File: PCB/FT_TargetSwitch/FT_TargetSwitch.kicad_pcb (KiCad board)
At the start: 2 copper layers, 73 x 73 mm, 11 parts

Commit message: changed hall, switch
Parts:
- R_PUP1: footprint Resistor_SMD:R_0603_1608Metric_Pad0.98x0.95mm_HandSolder -> Resistor_SMD:R_1206_3216Metric_Pad1.30x1.75mm_HandSolder
- moved D1 26.7 mm to (149.9, 78.7), turned to 180 degrees
- moved D2 14.2 mm to (128.3, 78.7), turned to 0 degrees
- moved Q_OUT1 11.5 mm to (142.2, 78.7), turned to 0 degrees
- moved R_PUP1 2.54 mm to (138.4, 71.1)
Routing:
- net /PASTRHRU_IN: track 7.61 -> 35.7 mm
- net /PASTHRU_OUT: track 68.6 -> 51.7 mm
- net /OUT: track 56.7 -> 69.3 mm
- net /HAL_IN: track 35.1 -> 25.9 mm
- net /Q_UOT_DRAIN: track 5.51 -> 4.18 mm
- net +12V: track 76.8 -> 75.9 mm
- removed copper zone on F.Cu, net GND

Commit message: update pcbs
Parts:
- removed D1, D2: M7, Diode_SMD:D_SMA_Handsoldering
- removed SW_L1, SW_R1: SW_DIP_x02, Button_Switch_THT:SW_DIP_SPSTx02_Slide_9.78x7.26mm_W7.62mm_P2.54mm
- R_PUP1: footprint Resistor_SMD:R_1206_3216Metric_Pad1.30x1.75mm_HandSolder -> Resistor_SMD:R_0603_1608Metric
- moved CON_PASTHRU1 53.2 mm to (126.7, 109.9)
- moved CON_LED1 52.1 mm to (113.6, 112.4)
- moved Q_LED1 50.7 mm to (109.0, 118.5)
- moved R_PUP1 49.7 mm to (117.6, 116.2), turned to 180 degrees
- moved Q_OUT1 47.9 mm to (117.6, 119.8), turned to 180 degrees
- moved CON_HAL1 43.1 mm to (113.7, 129.4)
- moved CON_IO1 41.8 mm to (126.8, 121.8)
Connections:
- CON_IO1 pad 3: /L_OUT -> /OUT
- CON_IO1 pad 4: /R_OUT -> /PASSTHRU_OUT
- CON_PASTHRU1 pad 3: /PASTRHRU_IN -> /PASSTHRU_OUT
- Q_OUT1 pad 3: /Q_UOT_DRAIN -> /OUT
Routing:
- net /OUT: track 69.3 -> 16.3 mm
- net /PASTHRU_OUT: track 51.7 -> 0.00 mm
- net /L_OUT: track 42.5 -> 0.00 mm
- net /PASSTHRU_OUT: track 0.00 -> 41.6 mm
- net /R_OUT: track 37.1 -> 0.00 mm
- net /PASTRHRU_IN: track 35.7 -> 0.00 mm
- net GND: track 0.00 -> 27.6 mm
- net /HAL_IN: track 25.9 -> 14.0 mm
- net +12V: track 75.9 -> 70.8 mm
- net /Q_UOT_DRAIN: track 4.18 -> 0.00 mm
- net /LED_OUT: track 9.95 -> 11.1 mm
- removed copper zone on B.Cu, net GND
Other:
- board size 73 x 73 mm -> 40 x 40 mm
- board text added: "Q1"
- board text added: "Q2"
- board text removed: ">L<"
- board text removed: ">R"
- board text removed: "Firesport timer | Light switch Martin Vejman v1"
- board text removed: "L"
- board text removed: "R"
- board text removed: "R<"

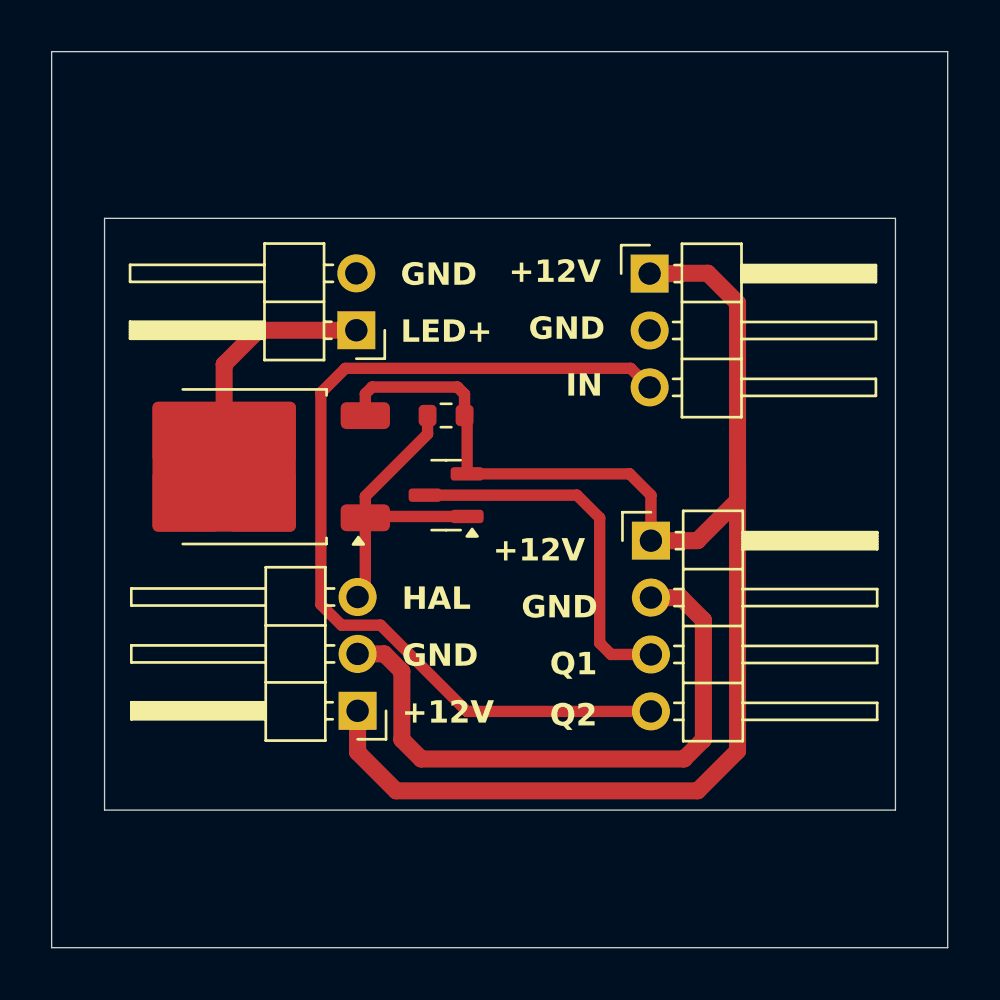
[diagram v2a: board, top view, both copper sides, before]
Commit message: hall and switch done
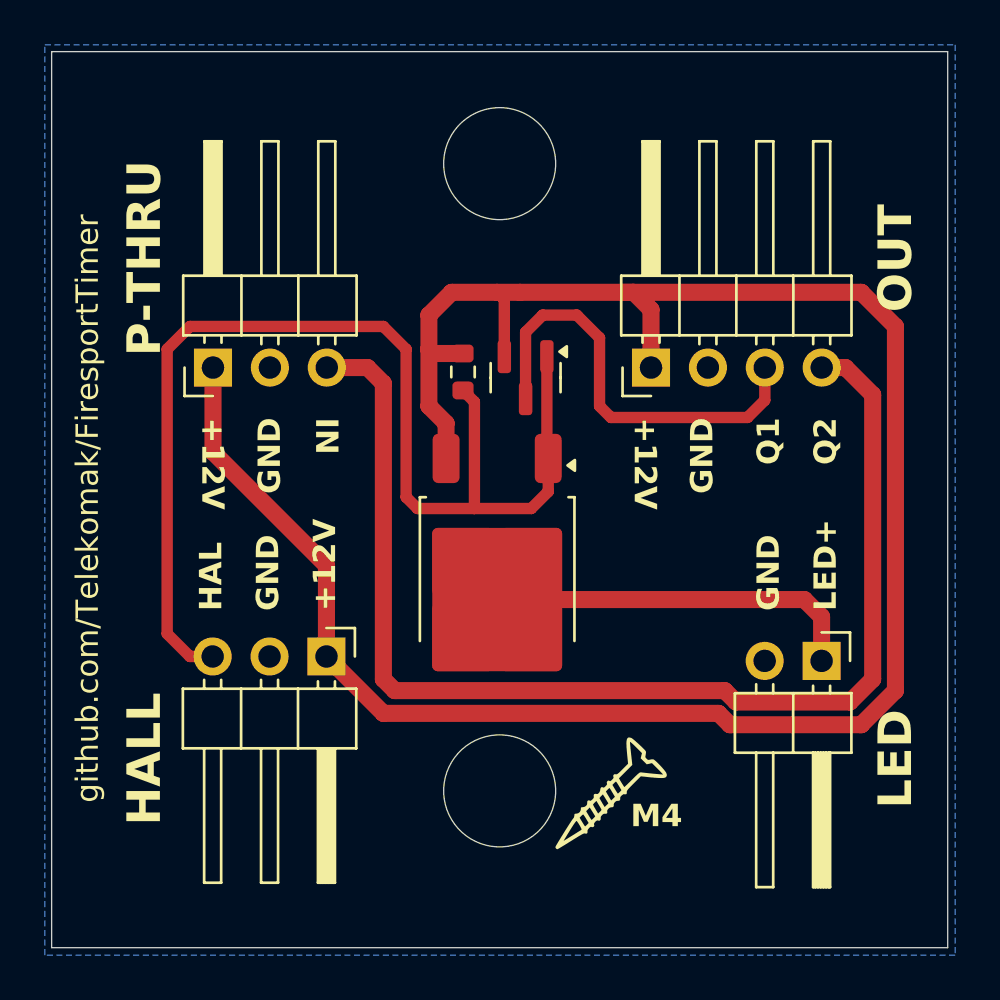
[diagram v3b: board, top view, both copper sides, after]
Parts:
- added G***: LOGO, LOGO, F.Cu at (125.0, 133.1)
- moved CON_LED1 25.5 mm to (134.4, 127.2), turned to -90 degrees
- moved CON_PASTHRU1 19.9 mm to (107.2, 114.1), turned to 90 degrees
- moved Q_LED1 11.9 mm to (119.9, 123.2), turned to -90 degrees
- moved CON_IO1 7.73 mm to (126.8, 114.1), turned to 90 degrees
- moved Q_OUT1 6.33 mm to (121.2, 114.6), turned to -90 degrees
- moved CON_HAL1 2.80 mm to (112.3, 127.0), turned to -90 degrees
- moved R_PUP1 2.08 mm to (118.4, 114.3), turned to -90 degrees
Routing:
- net /HAL_IN: track 14.0 -> 51.7 mm
- net GND: track 27.6 -> 0.00 mm
- net +12V: track 70.8 -> 95.9 mm
- net /PASSTHRU_OUT: track 41.6 -> 54.2 mm
- net /LED_OUT: track 11.1 -> 16.8 mm
- net /OUT: track 16.3 -> 19.4 mm
- added copper zone on B.Cu, net GND
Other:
- outline, holes or cut-outs redrawn
- board text added: "Firesport timer Light switch v1 Martin Vejman"
- board text added: "HALL"
- board text added: "LED"
- board text added: "M4"
- board text added: "OUT"
- board text added: "P-THRU"
- board text added: "github.com/Telekomak/FiresportTimer"

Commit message: final
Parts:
- renumbered CON_IO1 to CON1, CON_PASTHRU1 to CON2, CON_HAL1 to CON3, CON_LED1 to CON4, Q_OUT1 to Q1, Q_LED1 to Q1, R_PUP1 to R1
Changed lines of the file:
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@@
 		(descr "SOT, 3 Pin (https://www.jedec.org/system/files/docs/to-236h.pdf variant AB), generated with kicad-footprint-generator ipc_gullwing_generator.py")
 		(tags "SOT TO_SOT_SMD")
-		(property "Reference" "Q_OUT1"
+		(property "Reference" "Q1"
 			(at 2.794 1.016 180)
 			(layer "F.SilkS")
@@
 		(descr "Through hole angled pin header, 1x02, 2.54mm pitch, 6mm pin length, single row")
 		(tags "Through hole angled pin header THT 1x02 2.54mm single row")
-		(property "Reference" "CON_LED1"
+		(property "Reference" "CON4"
 			(at 4.375 7.625 90)
 			(layer "F.SilkS")
@@
 		(descr "Resistor SMD 0603 (1608 Metric), square (rectangular) end terminal, IPC_7351 nominal, (Body size source: IPC-SM-782 page 72, https://www.pcb-3d.com/wordpress/wp-content/uploads/ipc-sm-782a_amendment_1_and_2.pdf), generated with kicad-footprint-generator")
 		(tags "resistor")
-		(property "Reference" "R_PUP1"
+		(property "Reference" "R1"
 			(at 0 1.524 90)
 			(layer "F.SilkS")
@@
 		(descr "Through hole angled pin header, 1x03, 2.54mm pitch, 6mm pin length, single row")
 		(tags "Through hole angled pin header THT 1x03 2.54mm single row")
-		(property "Reference" "CON_PASTHRU1"
-			(at 4.375 -3.81 270)
+		(property "Reference" "CON2"
+			(at 4.375 -3.81 -90)
 			(layer "F.SilkS")
 			(hide yes)
@@
 		)
 		(property "Value" "Conn_01x03_Pin"
-			(at 4.385 7.35 270)
+			(at 4.385 7.35 -90)
 			(layer "F.Fab")
 			(hide yes)
@@
 		)
 		(fp_text user "${REFERENCE}"
-			(at 2.77 2.54 360)
+			(at 2.77 2.54 0)
 			(layer "F.Fab")
 			(effects
@@
 		(descr "TO-252/DPAK SMD package, http://www.infineon.com/cms/en/product/packages/PG-TO252/PG-TO252-3-1/")
 		(tags "DPAK TO-252 DPAK-3 TO-252-3 SOT-428")
-		(property "Reference" "Q_LED1"
+		(property "Reference" "Q1"
 			(at 5.578 0.254 180)
 			(layer "F.SilkS")
@@
 		(descr "Through hole angled pin header, 1x04, 2.54mm pitch, 6mm pin length, single row")
 		(tags "Through hole angled pin header THT 1x04 2.54mm single row")
-		(property "Reference" "CON_IO1"
-			(at 4.375 10.15 270)
+		(property "Reference" "CON1"
+			(at 4.375 10.15 -90)
 			(layer "F.SilkS")
 			(hide yes)
@@
 		)
 		(property "Value" "Conn_01x04_Pin"
-			(at 4.385 9.89 270)
+			(at 4.385 9.89 -90)
 			(layer "F.Fab")
 			(hide yes)
@@
 		)
 		(fp_text user "${REFERENCE}"
-			(at 2.77 3.81 360)
+			(at 2.77 3.81 0)
 			(layer "F.Fab")
 			(effects
@@
 		(descr "Through hole angled pin header, 1x03, 2.54mm pitch, 6mm pin length, single row")
 		(tags "Through hole angled pin header THT 1x03 2.54mm single row")
-		(property "Reference" "CON_HAL1"
+		(property "Reference" "CON3"
 			(at 4.375 -3.825 90)
 			(layer "F.SilkS")
@@
 		(polygon
 			(pts
-				(xy 99.695 99.695) (xy 140.335 99.695) (xy 140.335 140.335) (xy 99.695 140.335)
+				(xy 100 100) (xy 140 100) (xy 140 140) (xy 100 140)
 			)
 		)

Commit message: major changes, production ready
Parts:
- added F1: BSMD0603-025-12V, Fuse:Fuse_0603_1608Metric, F.Cu at (121.8, 110.8)
- Q1: value IRLML5203 -> 2N7002,215
- R1: value 100K -> 10K
- moved CON4 23.4 mm to (111.0, 127.0)
- moved CON3 21.7 mm to (134.0, 127.0)
- turned Q1 to 90 degrees
- renumbered Q1 to Q2
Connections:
- net /PASSTHRU_OUT renamed /PASSTHRU
- CON1 pad 1: +12V -> Net-(CON1-Pin_1)
- CON2 pad 1: +12V -> Net-(CON1-Pin_1)
- Q1 pad 2: +12V -> GND
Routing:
- net +12V: track 95.9 -> 38.9 mm
- net Net-(CON1-Pin_1): track 0.00 -> 33.6 mm
- net /HAL_IN: track 51.7 -> 19.6 mm
- net /LED_OUT: track 16.8 -> 5.75 mm, vias 0 -> 9
- net /OUT: track 19.4 -> 18.0 mm
- net GND: track 0.00 -> 1.15 mm, vias 0 -> 1
- added copper zone on B.Cu, net /LED_OUT
- added copper zone on F.Cu, net /LED_OUT

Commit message: panelization
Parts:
- renumbered CON1 to CON201, CON2 to CON202, CON3 to CON203, CON4 to CON204, F1 to F201, Q1 to Q201, Q2 to Q202, R1 to R201
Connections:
- CON201 pad 1: Net-(CON1-Pin_1) -> /OUT
- CON201 pad 3: /OUT -> /Q_UOT_DRAIN
- CON202 pad 1: Net-(CON1-Pin_1) -> /OUT
- F201 pad 1: Net-(CON1-Pin_1) -> /OUT
- Q201 pad 3: /OUT -> /Q_UOT_DRAIN
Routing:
- net Net-(CON1-Pin_1): track 33.6 -> 0.00 mm
- net /Q_UOT_DRAIN: track 0.00 -> 18.0 mm
- net /OUT: track 18.0 -> 33.6 mm
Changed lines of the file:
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@@
 	(net 4 "/LED_OUT")
 	(net 5 "/PASSTHRU")
-	(net 6 "Net-(CON1-Pin_1)")
+	(net 6 "/Q_UOT_DRAIN")
 	(net 7 "/OUT")
 	(footprint "Package_TO_SOT_SMD:SOT-23"
@@
 		(descr "SOT, 3 Pin (https://www.jedec.org/system/files/docs/to-236h.pdf variant AB), generated with kicad-footprint-generator ipc_gullwing_generator.py")
 		(tags "SOT TO_SOT_SMD")
-		(property "Reference" "Q1"
+		(property "Reference" "Q201"
 			(at 2.794 1.016 0)
 			(layer "F.SilkS")
@@
 			(layers "F.Cu" "F.Paste" "F.Mask")
 			(roundrect_rratio 0.25)
-			(net 7 "/OUT")
+			(net 6 "/Q_UOT_DRAIN")
 			(pinfunction "D")
 			(pintype "passive")
@@
 		(descr "Through hole angled pin header, 1x02, 2.54mm pitch, 6mm pin length, single row")
 		(tags "Through hole angled pin header THT 1x02 2.54mm single row")
-		(property "Reference" "CON4"
+		(property "Reference" "CON204"
 			(at 4.375 7.625 90)
 			(layer "F.SilkS")
@@
 		(descr "Fuse SMD 0603 (1608 Metric), square (rectangular) end terminal, IPC_7351 nominal, (Body size source: http://www.tortai-tech.com/upload/download/2011102023233369053.pdf), generated with kicad-footprint-generator")
 		(tags "fuse")
-		(property "Reference" "F1"
+		(property "Reference" "F201"
 			(at 0 -1.43 180)
 			(layer "F.SilkS")
@@
 			(layers "F.Cu" "F.Paste" "F.Mask")
 			(roundrect_rratio 0.25)
-			(net 6 "Net-(CON1-Pin_1)")
+			(net 7 "/OUT")
 			(pintype "passive")
 		)
@@
 		(descr "Resistor SMD 0603 (1608 Metric), square (rectangular) end terminal, IPC_7351 nominal, (Body size source: IPC-SM-782 page 72, https://www.pcb-3d.com/wordpress/wp-content/uploads/ipc-sm-782a_amendment_1_and_2.pdf), generated with kicad-footprint-generator")
 		(tags "resistor")
-		(property "Reference" "R1"
+		(property "Reference" "R201"
 			(at 0 1.524 90)
 			(layer "F.SilkS")
@@
 		(descr "Through hole angled pin header, 1x03, 2.54mm pitch, 6mm pin length, single row")
 		(tags "Through hole angled pin header THT 1x03 2.54mm single row")
-		(property "Reference" "CON2"
+		(property "Reference" "CON202"
 			(at 4.375 -3.81 -90)
 			(layer "F.SilkS")
@@
 			(layers "*.Cu" "*.Mask")
 			(remove_unused_layers no)
-			(net 6 "Net-(CON1-Pin_1)")
+			(net 7 "/OUT")
 			(pinfunction "Pin_1")
 			(pintype "passive")
@@
 		(descr "TO-252/DPAK SMD package, http://www.infineon.com/cms/en/product/packages/PG-TO252/PG-TO252-3-1/")
 		(tags "DPAK TO-252 DPAK-3 TO-252-3 SOT-428")
-		(property "Reference" "Q2"
+		(property "Reference" "Q202"
 			(at 5.578 0.254 180)
 			(layer "F.SilkS")
@@
 		(descr "Through hole angled pin header, 1x04, 2.54mm pitch, 6mm pin length, single row")
 		(tags "Through hole angled pin header THT 1x04 2.54mm single row")
-		(property "Reference" "CON1"
+		(property "Reference" "CON201"
 			(at 4.375 10.15 -90)
 			(layer "F.SilkS")
@@
 			(layers "*.Cu" "*.Mask")
 			(remove_unused_layers no)
-			(net 6 "Net-(CON1-Pin_1)")
+			(net 7 "/OUT")
 			(pinfunction "Pin_1")
 			(pintype "passive")
@@
 			(layers "*.Cu" "*.Mask")
 			(remove_unused_layers no)
-			(net 7 "/OUT")
+			(net 6 "/Q_UOT_DRAIN")
 			(pinfunction "Pin_3")
 			(pintype "passive")
@@
 		(descr "Through hole angled pin header, 1x03, 2.54mm pitch, 6mm pin length, single row")
 		(tags "Through hole angled pin header THT 1x03 2.54mm single row")
-		(property "Reference" "CON3"
+		(property "Reference" "CON203"
 			(at 4.375 -3.825 90)
 			(layer "F.SilkS")
@@
 	)
 	(segment
-		(start 125.47 110.75)
-		(end 125.476 110.744)
+		(start 123.952 112.522)
+		(end 123.952 116.078)
 		(width 0.762)
 		(layer "F.Cu")
@@
 	)
 	(segment
-		(start 125.984 110.744)
-		(end 125.476 110.744)
+		(start 121.158 112.522)
+		(end 121.666 112.014)
 		(width 0.762)
 		(layer "F.Cu")
@@
 	)
 	(segment
-		(start 126.756 111.516)
-		(end 126.756 114.103)
+		(start 121.158 113.6165)
+		(end 121.158 112.522)
 		(width 0.762)
 		(layer "F.Cu")
@@
 	)
 	(segment
-		(start 122.5375 110.75)
-		(end 125.47 110.75)
+		(start 124.46 116.586)
+		(end 131.064 116.586)
 		(width 0.762)
 		(layer "F.Cu")
@@
 	)
 	(segment
-		(start 107.203 114.103)
-		(end 107.203 109.797)
+		(start 123.952 116.078)
+		(end 124.46 116.586)
 		(width 0.762)
 		(layer "F.Cu")
@@
 	)
 	(segment
-		(start 125.75 108.75)
-		(end 126.756 109.756)
+		(start 121.666 112.014)
+		(end 123.444 112.014)
 		(width 0.762)
 		(layer "F.Cu")
@@
 	)
 	(segment
-		(start 126.756 111.516)
-		(end 125.984 110.744)
+		(start 123.444 112.014)
+		(end 123.952 112.522)
 		(width 0.762)
 		(layer "F.Cu")
@@
 	)
 	(segment
-		(start 108.25 108.75)
-		(end 125.75 108.75)
+		(start 131.836 115.814)
+		(end 131.836 114.103)
 		(width 0.762)
 		(layer "F.Cu")
@@
 	)
 	(segment
-		(start 107.203 109.797)
-		(end 108.25 108.75)
+		(start 131.064 116.586)
+		(end 131.836 115.814)
 		(width 0.762)
 		(layer "F.Cu")
@@
 	)
 	(segment
-		(start 126.756 109.756)
-		(end 126.756 111.516)
+		(start 125.47 110.75)
+		(end 125.476 110.744)
 		(width 0.762)
 		(layer "F.Cu")
-		(net 6)
+		(net 7)
 	)
 	(segment
-		(start 123.952 112.522)
-		(end 123.952 116.078)
+		(start 125.984 110.744)
+		(end 125.476 110.744)
 		(width 0.762)
 		(layer "F.Cu")
@@
 	)
 	(segment
-		(start 121.158 112.522)
-		(end 121.666 112.014)
+		(start 126.756 111.516)
+		(end 126.756 114.103)
 		(width 0.762)
 		(layer "F.Cu")
@@
 	)
 	(segment
-		(start 121.158 113.6165)
-		(end 121.158 112.522)
+		(start 122.5375 110.75)
+		(end 125.47 110.75)
 		(width 0.762)
 		(layer "F.Cu")
@@
 	)
 	(segment
-		(start 124.46 116.586)
-		(end 131.064 116.586)
+		(start 107.203 114.103)
+		(end 107.203 109.797)
 		(width 0.762)
 		(layer "F.Cu")
@@
 	)
 	(segment
-		(start 123.952 116.078)
-		(end 124.46 116.586)
+		(start 125.75 108.75)
+		(end 126.756 109.756)
 		(width 0.762)
 		(layer "F.Cu")
@@
 	)
 	(segment
-		(start 121.666 112.014)
-		(end 123.444 112.014)
+		(start 126.756 111.516)
+		(end 125.984 110.744)
 		(width 0.762)
 		(layer "F.Cu")
@@
 	)
 	(segment
-		(start 123.444 112.014)
-		(end 123.952 112.522)
+		(start 108.25 108.75)
+		(end 125.75 108.75)
 		(width 0.762)
 		(layer "F.Cu")
@@
 	)
 	(segment
-		(start 131.836 115.814)
-		(end 131.836 114.103)
+		(start 107.203 109.797)
+		(end 108.25 108.75)
 		(width 0.762)
 		(layer "F.Cu")
@@
 	)
 	(segment
-		(start 131.064 116.586)
-		(end 131.836 115.814)
+		(start 126.756 109.756)
+		(end 126.756 111.516)
 		(width 0.762)
 		(layer "F.Cu")
